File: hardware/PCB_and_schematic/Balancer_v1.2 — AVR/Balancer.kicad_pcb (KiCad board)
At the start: 2 copper layers, 99.5 x 99.5 mm, 198 parts, among them J1 BATT_OUT, J10 RS485, J11 HEATSING_TEMP1, J12 External Current Shunt, J13 BATT_IN, J14 LOAD_RESISTOR, J15 LOAD_RESISTOR, J16 ICP, J2 VOLTAGE_3WIRE, J3 Conn_01x03, J4 HEATSING_TEMP1, J5 FAN1, J6 FAN2, J7 BATT_12V, J9 RS485, Q1 BC817, Q10 BC807, Q11 BC817, Q12 BC817, Q13 BD238, Q14 BC807, Q15 BC817, Q16 BD238, Q17 BC817, Q18 IRF540N, Q19 BC817, Q2 BC337, Q20 BC817, Q21 BC817, Q22 BC817, Q23 BC817, Q25 IRF540N, Q3 BC327, Q4 PMOS, Q5 PMOS, Q6 BC337, Q7 BC327, Q8 BC817, Q9 BC817, U1 LM324, U10 PC817, U2 74AHCT125, U3 LM358, U4 TL432DBZ, U5 ADUM3211ARZ, U6 ST485, U7 INA226, U8 AVR64DD28, U9 B0505S-1W

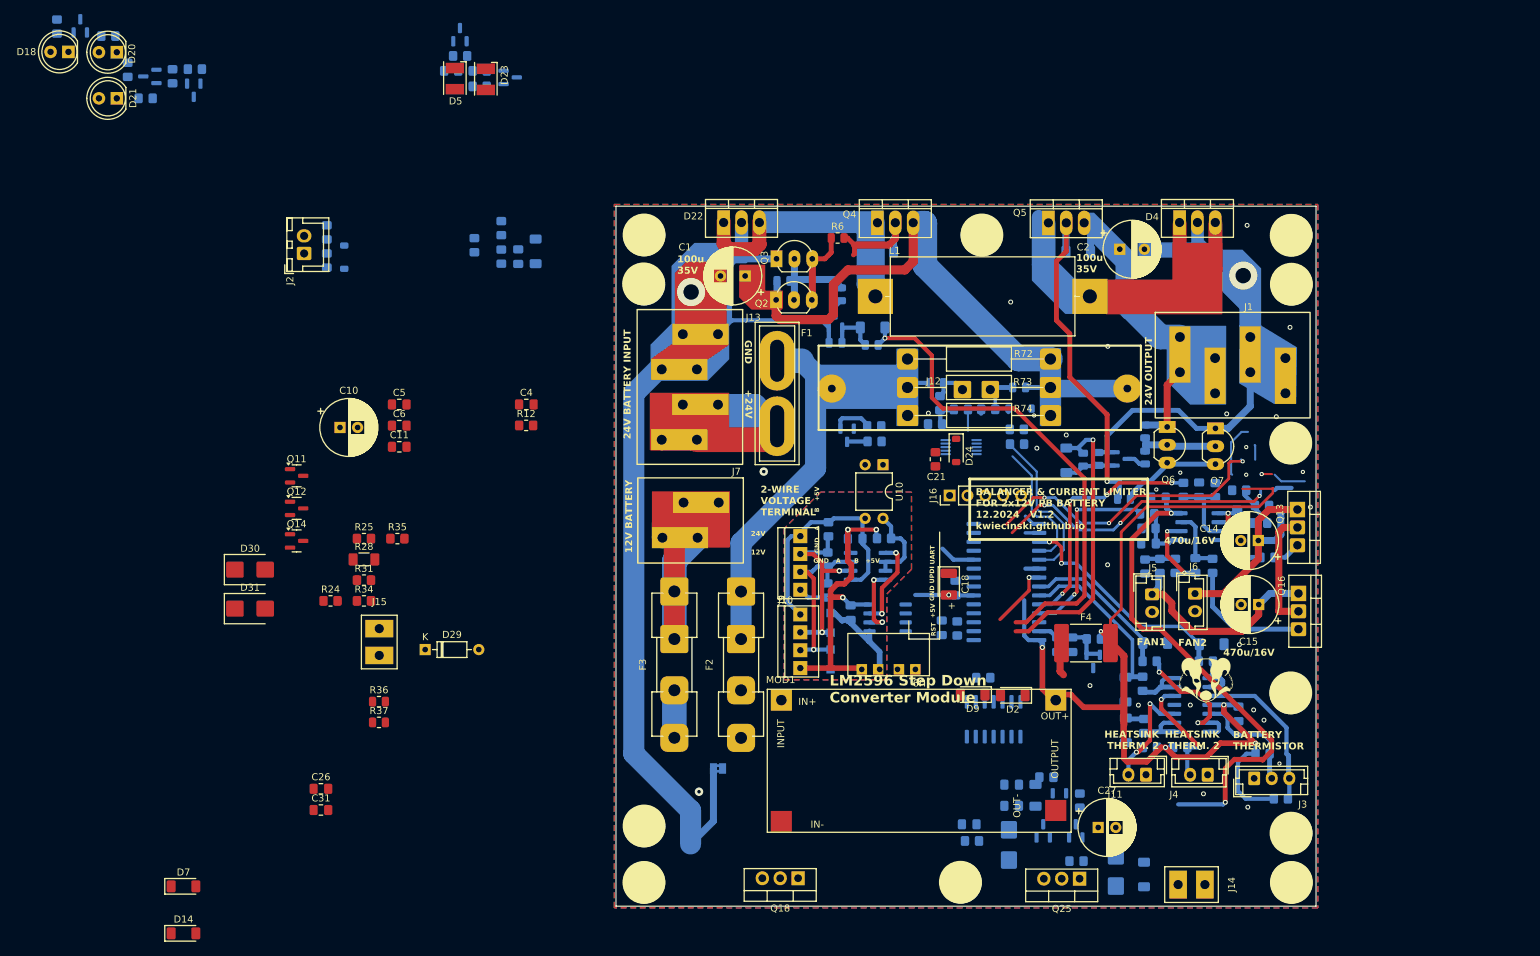
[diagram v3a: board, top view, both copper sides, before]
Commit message: Balancer PCB routing
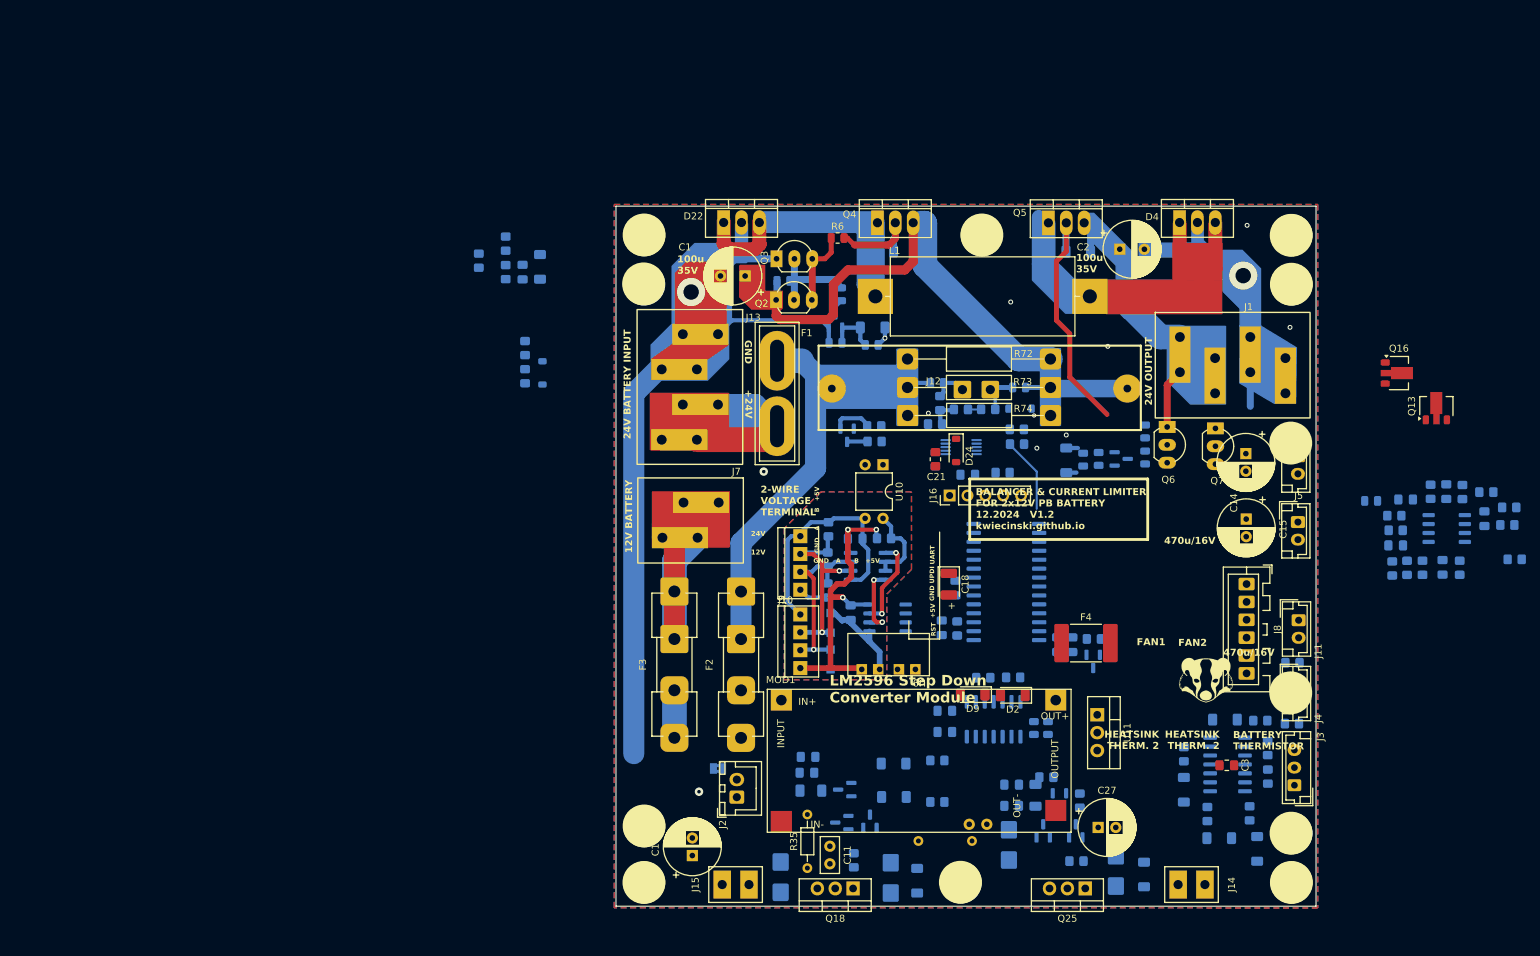
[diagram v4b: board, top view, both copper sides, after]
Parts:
- removed D18, D20, D21: LED, LED_THT:LED_D5.0mm
- removed D23, D5: LED, LED_SMD:LED_PLCC-2_3.4x3.0mm_KA
- removed Q17, Q19, Q20, Q21, Q22: BC817, Package_TO_SOT_SMD:SOT-23
- removed R56, R60, R62, R77, R79: 10K, Resistor_SMD:R_0805_2012Metric_Pad1.20x1.40mm_HandSolder
- removed R57, R61, R63, R78, R80: 220R, Resistor_SMD:R_0805_2012Metric_Pad1.20x1.40mm_HandSolder
- added J8: Conn_01x06, My-Footprints-connectors:JST_XH_1x06_P2.54mm_Vertical, F.Cu at (246.6, 104.8)
- added U11: LM7805_TO220, Package_TO_SOT_THT:TO-220-3_Vertical, F.Cu at (225.4, 123.2)
- C11, C30: footprint Capacitor_SMD:C_0805_2012Metric_Pad1.18x1.45mm_HandSolder -> Capacitor_THT:C_Disc_D5.0mm_W2.5mm_P2.50mm
- C26, C31, C4, C5, C6, D14, D30, D31, D7, Q11, Q12, Q14, R12, R24, R25, R28, R31, R34, R36, R37: moved to B.Cu
- C3: moved to F.Cu
- D29: footprint Diode_THT:D_DO-35_SOD27_P7.62mm_Horizontal -> Diode_SMD:D_MiniMELF; moved to B.Cu
- Q13, Q16: footprint My-Footprints:TO-220-3_Vertical-little-bigger pads -> Package_TO_SOT_SMD:SOT-89-3
- R35, R81: footprint Resistor_SMD:R_0805_2012Metric_Pad1.20x1.40mm_HandSolder -> Resistor_THT:R_Axial_DIN0204_L3.6mm_D1.6mm_P7.62mm_Horizontal
- moved D14 103.8 mm to (196.4, 130.1), turned to 180 degrees
- moved D7 101.8 mm to (196.5, 134.8), turned to 180 degrees
- moved D30 101.1 mm to (196.1, 146.3), turned to 90 degrees
- moved J2 98.8 mm to (174.2, 134.9)
- moved R24 97.6 mm to (213.4, 117.8), turned to 180 degrees
- moved R36 95.2 mm to (218.4, 125.0), turned to -90 degrees
- moved R37 93.1 mm to (216.4, 125.0), turned to -90 degrees
- moved Q12 92.8 mm to (193.1, 138.3), turned to 90 degrees
- moved Q11 89.8 mm to (189.5, 133.8), turned to 180 degrees
- moved C26 89.4 mm to (203.7, 122.6), turned to 180 degrees
- moved C31 89.4 mm to (203.7, 125.6), turned to 180 degrees
- moved R25 87.4 mm to (202.7, 129.7), turned to 180 degrees
- moved R31 87.4 mm to (202.7, 135.6), turned to 180 degrees
- moved Q14 87.2 mm to (189.1, 138.5), turned to 180 degrees
- moved D31 84.5 mm to (180.4, 146.2), turned to -90 degrees
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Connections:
- C18 pad 1: GND -> +12V_LOCAL
- C18 pad 2: +5V -> GND
- F4 pad 2: +5V -> +12V_LOCAL
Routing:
- net +5V: track 157.3 -> 0.00 mm, vias 6 -> 0
- net +BATT_24V: track 70.6 -> 0.00 mm, vias 2 -> 0
- net Net-(D1-K): track 71.0 -> 2.88 mm
- net GNDA: track 163.8 -> 106.7 mm
- net LED3_PA6: track 41.9 -> 0.00 mm, vias 3 -> 0
- net LED4_PA5: track 41.1 -> 0.00 mm, vias 3 -> 0
- net Net-(D8-K): track 40.8 -> 1.66 mm, vias 1 -> 0
- net PWM_OUT2: track 34.7 -> 0.00 mm, vias 4 -> 0
- net Net-(J6-Pin_1): track 34.3 -> 0.00 mm
- net TEMP_AKU_12V: track 32.6 -> 0.00 mm, vias 2 -> 0
- net Net-(J5-Pin_1): track 30.1 -> 0.00 mm
- net PWM_OUT1: track 27.6 -> 0.00 mm, vias 2 -> 0
- net TEMP_HEAT_SINK_24V: track 24.7 -> 0.00 mm
- net Net-(J3-Pin_3): track 23.3 -> 0.00 mm
- net TEMP_AKU_24V: track 21.9 -> 0.00 mm
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
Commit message: Update balacer schematic - change fan drive circuit,  fix current limiter drive
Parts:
- removed D8: LL4148, Diode_SMD:D_MiniMELF
- removed J2: VOLTAGE_3WIRE, Connector_JST:JST_XH_B2B-XH-A_1x02_P2.50mm_Vertical
- removed U3: LM358, Package_SO:SO-8_3.9x4.9mm_P1.27mm
- added C33: 100u/25V, Capacitor_THT:CP_Radial_D8.0mm_P2.50mm, F.Cu at (300.0, 60.1)
- added C34: 220u/35V, Capacitor_THT:CP_Radial_D8.0mm_P2.50mm, F.Cu at (300.0, 69.7)
- added C35: 220u/6,3V, Capacitor_THT:CP_Radial_D8.0mm_P2.50mm, F.Cu at (300.0, 79.2)
- added C36: 470u/16V, Capacitor_THT:CP_Radial_D8.0mm_P2.50mm, F.Cu at (300.0, 88.8)
- added C37: 100n, Capacitor_SMD:C_0805_2012Metric_Pad1.18x1.45mm_HandSolder, F.Cu at (319.9, 50.9)
- added C38: 1u, Capacitor_THT:C_Disc_D5.0mm_W2.5mm_P2.50mm, F.Cu at (328.1, 78.1)
- added C39: 100n, Capacitor_SMD:C_0805_2012Metric_Pad1.18x1.45mm_HandSolder, F.Cu at (319.9, 53.9)
- added C40: 100n, Capacitor_SMD:C_0805_2012Metric_Pad1.18x1.45mm_HandSolder, F.Cu at (377.2, 80.4)
- added D5: SM6T15A, Diode_SMD:D_SMB, F.Cu at (321.9, 80.3)
- added R56: 1k, Resistor_SMD:R_0805_2012Metric_Pad1.20x1.40mm_HandSolder, F.Cu at (308.4, 56.8)
- added R57: 1k, Resistor_SMD:R_0805_2012Metric_Pad1.20x1.40mm_HandSolder, F.Cu at (308.4, 59.8)
- added R60: 10k/1%, Resistor_SMD:R_0805_2012Metric_Pad1.20x1.40mm_HandSolder, F.Cu at (315.1, 50.9)
- added R61: 10k/1%, Resistor_SMD:R_0805_2012Metric_Pad1.20x1.40mm_HandSolder, F.Cu at (315.1, 53.8)
- added R62: 10k/1%, Resistor_SMD:R_0805_2012Metric_Pad1.20x1.40mm_HandSolder, F.Cu at (315.1, 56.8)
- added R63: 10k/1%, Resistor_SMD:R_0805_2012Metric_Pad1.20x1.40mm_HandSolder, F.Cu at (315.1, 59.7)
- added R66: 10k/1%, Resistor_SMD:R_0805_2012Metric_Pad1.20x1.40mm_HandSolder, F.Cu at (315.1, 62.6)
- added R67: 10k/1%, Resistor_SMD:R_0805_2012Metric_Pad1.20x1.40mm_HandSolder, F.Cu at (315.1, 65.6)
- added R68: 10R, Resistor_THT:R_Axial_DIN0204_L3.6mm_D1.6mm_P7.62mm_Horizontal, F.Cu at (319.1, 84.7)
- added R71: 100R, Resistor_SMD:R_0805_2012Metric_Pad1.20x1.40mm_HandSolder, F.Cu at (315.1, 68.5)
- added R77: 10R, Resistor_THT:R_Axial_DIN0204_L3.6mm_D1.6mm_P7.62mm_Horizontal, F.Cu at (319.1, 87.8)
- added U12: LM317_TO-220, Package_TO_SOT_THT:TO-220-3_Vertical, F.Cu at (299.5, 53.3)
- C7: value 100n -> 1u; footprint Capacitor_SMD:C_0805_2012Metric_Pad1.18x1.45mm_HandSolder -> Capacitor_THT:C_Disc_D5.0mm_W2.5mm_P2.50mm; moved to F.Cu
- D1: value LL4148 -> SM6T15A; footprint Diode_SMD:D_MiniMELF -> Diode_SMD:D_SMB; moved to F.Cu
- D22, D4: value D_Schottky_Dual_CommonAnode_KAK_Parallel -> D_Schottky
- Q2, Q6: value BC337 -> BC817; footprint My-Footprints:TO-92_Inline_Wide -> Package_TO_SOT_SMD:SOT-23
- Q3, Q7: value BC327 -> BC807; footprint My-Footprints:TO-92_Inline_Wide -> Package_TO_SOT_SMD:SOT-23
- R1, R11: value 4k7 -> 1k
- R10, R2: value 10k -> 100R; moved to F.Cu
- R3, R8: footprint Resistor_SMD:R_0805_2012Metric -> Resistor_SMD:R_1206_3216Metric
- moved R2 143.0 mm to (330.4, 84.6)
- moved Q3 137.0 mm to (315.2, 79.0)
- moved Q2 135.8 mm to (315.2, 74.4)
- moved D1 128.6 mm to (321.9, 74.8), turned to 0 degrees
- moved C15 106.7 mm to (350.2, 120.7)
- moved J6 106.7 mm to (357.6, 111.8)
- moved C14 106.7 mm to (350.2, 111.4)
- moved J5 106.7 mm to (357.6, 121.1)
- moved R10 104.8 mm to (330.4, 87.5), turned to 0 degrees
- moved Q6 79.9 mm to (315.2, 83.7), turned to 0 degrees
- moved Q7 73.3 mm to (315.2, 88.3), turned to 0 degrees
- moved Q16 68.8 mm to (332.0, 100.7)
- moved Q13 68.8 mm to (337.3, 105.4)
- moved R29 61.9 mm to (330.1, 114.9)
- moved C12 61.9 mm to (337.8, 118.8)
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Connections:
- C1 pad 1: Net-(D3-K) -> Net-(D1-A1)
- C11 pad 2: Net-(D29-A) -> GNDA
- C28 pad 1: +BATT_24V -> +24V_LOCAL
- C29 pad 1: +BATT_24V -> +24V_LOCAL
- C5 pad 1: +BATT_12V -> +12V_LOCAL
- C6 pad 1: +BATT_12V -> +12V_LOCAL
- C7 pad 1: +BATT_24V -> Net-(C7-Pad1)
- C7 pad 2: GND -> Net-(D1-A2)
- D1 pad 1: Net-(D1-K) -> Net-(D1-A1)
- D1 pad 2: Net-(D1-A) -> Net-(D1-A2)
- D22 pad 1: Net-(Q4-D) -> Net-(D1-A2)
- D22 pad 3: Net-(Q4-D) -> Net-(D1-A2)
- D29 pad 2: Net-(D29-A) -> GNDA
- D3 pad 1: Net-(D3-K) -> Net-(D1-A1)
- D30 pad 2: Net-(D29-A) -> GNDA
- D31 pad 2: Net-(D29-A) -> GNDA
- L1 pad 1: Net-(Q4-D) -> Net-(D1-A2)
- Q1 pad 1: Net-(D1-A) -> Net-(Q1-B)
- Q1 pad 2: GNDA -> Net-(Q1-E)
- Q12 pad 3: +BATT_12V -> +12V_LOCAL
- Q18 pad 3: Net-(D29-A) -> GNDA
- Q2 pad 1: Net-(D3-K) -> Net-(Q2-B)
- Q2 pad 2: Net-(Q2-B) -> Net-(Q2-E)
- Q2 pad 3: Net-(Q2-E) -> Net-(D1-A1)
- Q3 pad 1: GNDA -> Net-(Q2-B)
- Q3 pad 2: Net-(Q2-B) -> Net-(Q2-E)
- Q3 pad 3: Net-(Q2-E) -> +12V_LOCAL
- Q4 pad 1: Net-(Q4-D) -> Net-(D1-A2)
- Q4 pad 3: Net-(D3-K) -> Net-(D1-A1)
- Q6 pad 1: DC_LINE_24V -> Net-(Q6-B)
- Q6 pad 2: Net-(Q6-B) -> Net-(Q6-E)
- Q6 pad 3: Net-(Q6-E) -> DC_LINE_24V
- Q7 pad 1: GNDA -> Net-(Q6-B)
- Q7 pad 2: Net-(Q6-B) -> Net-(Q6-E)
- Q7 pad 3: Net-(Q6-E) -> +12V_LOCAL
- Q8 pad 1: Net-(D8-A) -> Net-(Q8-B)
- Q8 pad 2: GNDA -> Net-(Q8-E)
- Q9 pad 3: +BATT_24V -> +24V_LOCAL
- R1 pad 1: Net-(D1-K) -> Net-(R1-Pad1)
- R1 pad 2: Net-(D1-A) -> Net-(Q1-B)
- R10 pad 1: GNDA -> Net-(Q8-E)
- R10 pad 2: Net-(D8-A) -> GNDA
- R11 pad 2: Net-(D8-A) -> Net-(Q8-B)
- R2 pad 2: Net-(D1-A) -> Net-(Q1-E)
- R28 pad 1: +BATT_12V -> +12V_LOCAL
- R3 pad 2: Net-(D3-K) -> Net-(D1-A1)
- R36 pad 2: +5V -> GND
- R37 pad 2: +5V -> GND
- R5 pad 2: Net-(D3-K) -> Net-(D1-A1)
- R69 pad 1: +BATT_24V -> +24V_LOCAL
- R72 pad 2: Net-(D3-K) -> Net-(D1-A1)
- R73 pad 2: Net-(D3-K) -> Net-(D1-A1)
- R74 pad 2: Net-(D3-K) -> Net-(D1-A1)
- R76 pad 1: Net-(D3-K) -> Net-(D1-A1)
- U2 pad 8: Net-(D1-K) -> Net-(R1-Pad1)
- U8 pad 28: LED3_PA6 -> GND_VOLTAGE_DROP_ADC
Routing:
- net GNDA: track 106.7 -> 18.4 mm, vias 2 -> 1
- net Net-(D3-K): track 85.8 -> 0.00 mm
- net Net-(D1-A1): track 0.00 -> 49.8 mm
- net Net-(Q4-D): track 43.5 -> 0.00 mm
- net Net-(D1-A2): track 0.00 -> 43.5 mm
- net Net-(D6-A): track 34.9 -> 4.12 mm
- net Net-(D3-A): track 15.0 -> 0.00 mm
- net Net-(Q2-B): track 12.5 -> 0.00 mm
- net Net-(Q2-E): track 10.8 -> 0.00 mm
- net CLOCK: track 10.7 -> 0.00 mm
- net DC_LINE_24V: track 21.1 -> 12.5 mm
- net Net-(D1-A): track 7.53 -> 0.00 mm
- net Net-(Q5-D): track 63.2 -> 58.2 mm
- net Net-(D1-K): track 2.88 -> 0.00 mm, vias 1 -> 0
- net Net-(Q1-C): track 2.28 -> 0.00 mm
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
